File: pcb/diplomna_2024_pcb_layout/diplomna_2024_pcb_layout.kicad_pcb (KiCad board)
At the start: 4 copper layers, 10 parts

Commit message: pcb
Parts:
- added REF**: R_Axial_DIN0204_L3.6mm_D1.6mm_P5.08mm_Horizontal, Resistor_THT:R_Axial_DIN0204_L3.6mm_D1.6mm_P5.08mm_Horizontal, F.Cu at (191.0, 75.5)
- added REF**: R_Axial_DIN0204_L3.6mm_D1.6mm_P5.08mm_Horizontal, Resistor_THT:R_Axial_DIN0204_L3.6mm_D1.6mm_P5.08mm_Horizontal, F.Cu at (195.5, 78.5)
- moved REF** 58.6 mm to (238.0, 138.4), turned to 180 degrees
- moved REF** 58.6 mm to (204.5, 138.4), turned to 180 degrees
- moved REF** 58.6 mm to (201.5, 138.4), turned to 180 degrees
- moved REF** 58.5 mm to (221.0, 138.4), turned to 180 degrees
- moved REF** 58.4 mm to (186.0, 138.4), turned to 180 degrees
- moved REF** 58.3 mm to (169.0, 138.4), turned to 180 degrees
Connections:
- REF** pad 17: (no net) -> CS (x2)
- REF** pad 24: (no net) -> VDD
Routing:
- net (no net): track 0.00 -> 632.6 mm
- net CS: track 0.00 -> 36.3 mm
- net VDD: track 0.00 -> 15.2 mm
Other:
- board outline added: 95 x 95 mm
- board text added: "CS"
- board text added: "MISO"
- board text added: "MOSI"
- board text added: "SCL"
- board text added: "SDA"
- board text added: "analog"

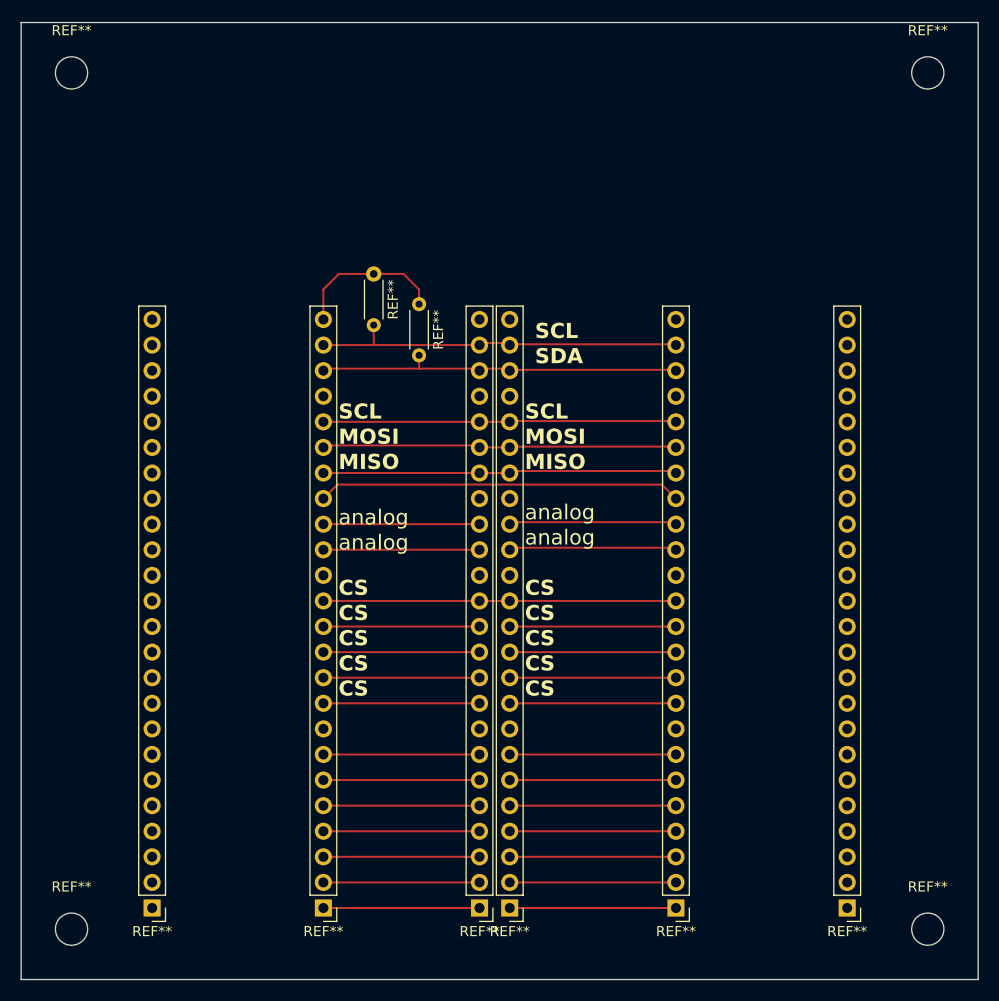
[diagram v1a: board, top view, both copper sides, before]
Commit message: pcb design changes
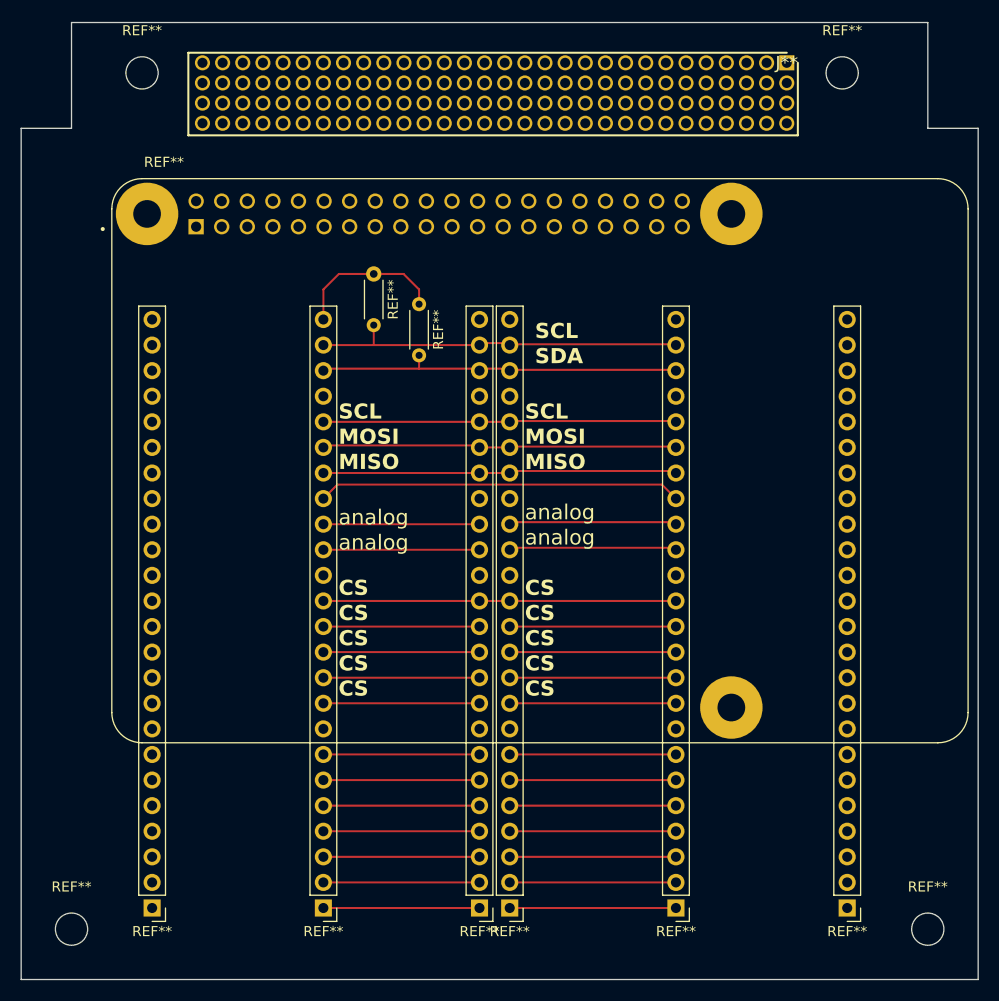
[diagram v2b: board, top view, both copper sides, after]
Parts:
- added J**: RHDR120W55P200_4X30_6020X800X935P, KiCad:RHDR120W55P200_4X30_6020X800X935P, F.Cu at (232.0, 54.5)
- added REF**: MODULE_SC0194_9_, raspberry pi4:MODULE_SC0194_9_, F.Cu at (207.5, 94.0)
- moved REF** 8.50 mm to (237.5, 55.5)
- moved REF** 7.00 mm to (168.0, 55.5)
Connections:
- REF** pad 24: (no net) -> GND (x2)
- REF** pad 24: (no net) -> VDD
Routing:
- added copper zone on In1.Cu, net GND
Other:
- outline, holes or cut-outs redrawn

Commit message: pcb final changes
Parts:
- added ?: , , F.Cu at (161.0, 118.5)
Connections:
- J** pad 100: (no net) -> I/O
- J** pad 101: (no net) -> I/O
- J** pad 102: (no net) -> I/O
- J** pad 107: (no net) -> I/O
- J** pad 108: (no net) -> I/O
- J** pad 109: (no net) -> I/O
- J** pad 110: (no net) -> I/O
- J** pad 111: (no net) -> I/O
- J** pad 112: (no net) -> I/O
- J** pad 114: (no net) -> rx
- J** pad 115: (no net) -> tx
- J** pad 117: (no net) -> scl_i2c
- J** pad 118: (no net) -> sda_i2c
- J** pad 120: (no net) -> VDD
- J** pad 30: (no net) -> GND
- J** pad 60: (no net) -> 3.3v
- J** pad 90: (no net) -> VDD
- REF** pad 1: (no net) -> I/O (x4)
- REF** pad 10: (no net) -> CS (x4)
- REF** pad 11: (no net) -> CS (x4)
- REF** pad 12: (no net) -> CS (x4)
- REF** pad 13: (no net) -> CS (x4)
- REF** pad 15: (no net) -> analog (x4)
- REF** pad 16: (no net) -> analog (x4)
- REF** pad 18: (no net) -> miso (x4)
- REF** pad 19: (no net) -> mosi (x5)
- REF** pad 2: (no net) -> I/O (x4)
- REF** pad 20: (no net) -> scl (x4)
- REF** pad 22: (no net) -> sda_i2c (x4)
- REF** pad 23: (no net) -> scl_i2c (x4)
- REF** pad 3: (no net) -> I/O (x4)
- REF** pad 4: (no net) -> I/O (x4)
- REF** pad 5: (no net) -> I/O (x4)
- REF** pad 6: (no net) -> I/O (x4)
- REF** pad 7: (no net) -> I/O (x4)
- REF** pad 9: (no net) -> CS (x4)
- REF** pad 2: (no net) -> scl_i2c
- REF** pad 3: (no net) -> sda_i2c (x2)
- REF** pad 1: (no net) -> 3.3v
- REF** pad 10: (no net) -> rx
- REF** pad 16: (no net) -> I/O
- REF** pad 18: (no net) -> I/O
- REF** pad 2: (no net) -> VDD
- REF** pad 21: (no net) -> miso
- REF** pad 22: (no net) -> I/O
- REF** pad 23: (no net) -> scl
- REF** pad 24: (no net) -> I/O
- REF** pad 26: (no net) -> I/O
- REF** pad 28: (no net) -> I/O
- REF** pad 36: (no net) -> I/O
- REF** pad 38: (no net) -> I/O
- REF** pad 4: (no net) -> VDD
- REF** pad 40: (no net) -> I/O
- REF** pad 5: (no net) -> scl_i2c
- REF** pad 8: (no net) -> tx
- REF** pad S1: (no net) -> GND
- REF** pad S2: (no net) -> GND
- REF** pad S3: (no net) -> GND
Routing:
- net (no net): track 632.6 -> 0.00 mm
- net I/O: track 0.00 -> 312.8 mm
- net CS: track 36.3 -> 199.3 mm
- net miso: track 0.00 -> 82.7 mm
- net mosi: track 0.00 -> 80.7 mm
- net scl: track 0.00 -> 77.6 mm, vias 0 -> 1
- net sda_i2c: track 0.00 -> 66.5 mm
- net analog: track 0.00 -> 64.3 mm
- net scl_i2c: track 0.00 -> 63.4 mm
- net VDD: track 15.2 -> 33.7 mm
- net 3.3v: track 0.00 -> 15.4 mm
- net tx: track 0.00 -> 8.98 mm
- net rx: track 0.00 -> 8.75 mm

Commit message: pc design updates
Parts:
- moved REF** 2.00 mm to (171.0, 138.4)
- moved REF** 2.00 mm to (236.0, 138.4)
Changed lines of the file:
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@@
 			(drillshape 0)
 			(scaleselection 1)
-			(outputdirectory "./")
+			(outputdirectory "v3/")
 		)
 	)
@@
 	(footprint "Connector_PinHeader_2.54mm:PinHeader_1x24_P2.54mm_Vertical"
 		(layer "F.Cu")
-		(at 238 138.4 180)
+		(at 236 138.4 180)
 		(descr "Through hole straight pin header, 1x24, 2.54mm pitch, single row")
 		(tags "Through hole pin header THT 1x24 2.54mm single row")
@@
 	(footprint "Connector_PinHeader_2.54mm:PinHeader_1x24_P2.54mm_Vertical"
 		(layer "F.Cu")
-		(at 169 138.4 180)
+		(at 171 138.42 180)
 		(descr "Through hole straight pin header, 1x24, 2.54mm pitch, single row")
 		(tags "Through hole pin header THT 1x24 2.54mm single row")
@@
 		(net 9)
 	)
-	(via micro
+	(via
 		(at 205 75.5)
-		(size 0.3)
-		(drill 0.1)
-		(layers "F.Cu" "In2.Cu")
+		(size 0.6)
+		(drill 0.3)
+		(layers "F.Cu" "B.Cu")
 		(free yes)
 		(net 9)

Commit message: PC UPDATES
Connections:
- J** pad 1: (no net) -> GND
- J** pad 2: (no net) -> GND
- J** pad 31: (no net) -> GND
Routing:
- net VDD: track 33.7 -> 123.3 mm
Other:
- board text added: "v2"
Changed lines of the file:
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@@
 			(drillshape 0)
 			(scaleselection 1)
-			(outputdirectory "v3/")
+			(outputdirectory "vl/")
 		)
 	)
@@
 			(layers "*.Cu" "*.Mask")
 			(remove_unused_layers no)
+			(net 3 "GND")
 		)
 		(pad "2" thru_hole circle
@@
 			(layers "*.Cu" "*.Mask")
 			(remove_unused_layers no)
+			(net 3 "GND")
 		)
 		(pad "3" thru_hole circle
@@
 			(layers "*.Cu" "*.Mask")
 			(remove_unused_layers no)
+			(net 3 "GND")
 		)
 		(pad "32" thru_hole circle
@@
 		)
 	)
+	(gr_text "v2"
+		(at 247.5 63.5 0)
+		(layer "F.SilkS")
+		(effects
+			(font
+				(size 1 1)
+				(thickness 0.1)
+			)
+			(justify left bottom)
+		)
+	)
 	(gr_text "CS"
 		(at 187.5 115 0)
@@
 		(net 1)
 	)
+	(segment
+		(start 171.5 61)
+		(end 171.5 62.5)
+		(width 0.2)
+		(layer "In2.Cu")
+		(net 1)
+	)
+	(segment
+		(start 177 63.5)
+		(end 177 70.98)
+		(width 0.2)
+		(layer "In2.Cu")
+		(net 1)
+	)
+	(segment
+		(start 186 75.5)
+		(end 188.5 73)
+		(width 0.2)
+		(layer "In2.Cu")
+		(net 1)
+	)
+	(segment
+		(start 229.02 73)
+		(end 236 79.98)
+		(width 0.2)
+		(layer "In2.Cu")
+		(net 1)
+	)
+	(segment
+		(start 171.5 62.5)
+		(end 176 62.5)
+		(width 0.2)
+		(layer "In2.Cu")
+		(net 1)
+	)
+	(segment
+		(start 174 58.5)
+		(end 171.5 61)
+		(width 0.2)
+		(layer "In2.Cu")
+		(net 1)
+	)
+	(segment
+		(start 176 62.5)
+		(end 177 63.5)
+		(width 0.2)
+		(layer "In2.Cu")
+		(net 1)
+	)
+	(segment
+		(start 186 79.98)
+		(end 186 75.5)
+		(width 0.2)
+		(layer "In2.Cu")
+		(net 1)
+	)
+	(segment
+		(start 188.5 73)
+		(end 229.02 73)
+		(width 0.2)
+		(layer "In2.Cu")
+		(net 1)
+	)
+	(segment
+		(start 177 70.98)
+		(end 186 79.98)
+		(width 0.2)
+		(layer "In2.Cu")
+		(net 1)
+	)

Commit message: pcb chnge
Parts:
- removed ?: , 
- removed the REF** at (207.5, 94.0)
- added REF**: MODULE_CM4102008, rp1:MODULE_CM4102008, B.Cu at (228.5, 102.0)
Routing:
- net I/O: track 312.8 -> 175.2 mm
- net miso: track 82.7 -> 35.1 mm
- net mosi: track 80.7 -> 35.1 mm
- net scl: track 77.6 -> 35.7 mm, vias 1 -> 0
- net VDD: track 123.3 -> 107.0 mm
- net 3.3v: track 15.4 -> 0.00 mm
- net tx: track 8.98 -> 0.00 mm
- net rx: track 8.75 -> 0.00 mm

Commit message: testing and presentation changes
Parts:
- removed the REF** at (191.0, 75.5)
- removed the REF** at (195.5, 78.5)
- removed the REF** at (204.5, 138.4)
- removed the REF** at (201.5, 138.4)
- REF**: moved to F.Cu
- moved REF** 23.0 mm to (243.5, 133.5), turned to -90 degrees
- moved REF** 21.3 mm to (243.5, 118.5), turned to -90 degrees
- moved REF** 17.5 mm to (218.0, 88.0), turned to 180 degrees
- moved REF** 13.8 mm to (177.5, 127.5)
- moved REF** 13.8 mm to (162.5, 127.6)
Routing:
- net CS: track 199.3 -> 0.00 mm
- net I/O: track 175.2 -> 0.74 mm
- net VDD: track 107.0 -> 2.23 mm
- net sda_i2c: track 66.5 -> 0.87 mm
- net analog: track 64.3 -> 0.00 mm
- net scl_i2c: track 63.4 -> 0.10 mm
- net scl: track 35.7 -> 0.00 mm
- net miso: track 35.1 -> 0.00 mm
- net mosi: track 35.1 -> 0.00 mm
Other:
- board text removed: "SDA"
